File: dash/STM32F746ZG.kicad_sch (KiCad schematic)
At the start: 84 parts, among them J1 XF2M-4015-1A, J2 CLP-103-02-F-D, J4 TC2030, J5 MEM2061-01-188-00-A, J6 USB_C_Receptacle_USB2.0_16P, SW1 SW_SPST, SW2 PTS647Sx38, SW3 PTS647Sx38, U1 W9812G6KH-5, U2 STM32F746ZGTx, U7 XPT2046TS, Y2 25MHz

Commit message: nearly finished?
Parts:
- SW2, SW3: value PTS647Sx38 -> KMR221G LFS; footprint Button_Switch_SMD:SW_SPST_PTS647_Sx38 -> Button_Switch_SMD:SW_Push_1P1T_NO_CK_KMR2
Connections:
- net ~{USB_FAULT}: now also U2.80 (PD11); no longer U2.74 (PB13)
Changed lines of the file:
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@@
 	)
 	(no_connect
-		(at 370.84 219.71)
+		(at 304.8 92.71)
 	)
 	(no_connect
-		(at 304.8 92.71)
+		(at 370.84 138.43)
 	)
 	(no_connect
@@
 	(wire
 		(pts
+			(xy 370.84 219.71) (xy 377.19 219.71)
+		)
+		(stroke
+			(width 0)
+			(type default)
+		)
+	)
+	(wire
+		(pts
 			(xy 62.23 100.33) (xy 69.85 100.33)
 		)
@@
 	(wire
 		(pts
-			(xy 370.84 138.43) (xy 377.19 138.43)
-		)
-		(stroke
-			(width 0)
-			(type default)
-		)
-	)
-	(wire
-		(pts
 			(xy 377.19 168.91) (xy 370.84 168.91)
 		)
@@
 	(global_label "~{USB_FAULT}"
 		(shape input)
-		(at 377.19 138.43 0)
+		(at 377.19 219.71 0)
 		(fields_autoplaced yes)
 		(effects
@@
 		)
 		(property "Intersheetrefs" "${INTERSHEET_REFS}"
-			(at 389.802 138.43 0)
+			(at 389.802 219.71 0)
 			(effects
 				(font
@@
 			)
 		)
-		(property "Value" "PTS647Sx38"
+		(property "Value" "KMR221G LFS"
 			(at 270.383 278.638 90)
 			(effects
@@
 			)
 		)
-		(property "Footprint" "Button_Switch_SMD:SW_SPST_PTS647_Sx38"
+		(property "Footprint" "Button_Switch_SMD:SW_Push_1P1T_NO_CK_KMR2"
 			(at 276.86 267.97 0)
 			(effects
@@
 			)
 		)
-		(property "Value" "PTS647Sx38"
+		(property "Value" "KMR221G LFS"
 			(at 213.233 50.038 90)
 			(effects
@@
 			)
 		)
-		(property "Footprint" "Button_Switch_SMD:SW_SPST_PTS647_Sx38"
+		(property "Footprint" "Button_Switch_SMD:SW_Push_1P1T_NO_CK_KMR2"
 			(at 219.71 39.37 0)
 			(effects

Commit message: final stretch
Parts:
- SW1: footprint Button_Switch_SMD:SW_DIP_SPSTx01_Slide_Omron_A6S-110x_W8.9mm_P2.54mm -> Temp:A6T-1101
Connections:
- net user_button: now also U2.21 (PF9)
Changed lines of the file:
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@@
 	)
 	(no_connect
+		(at 370.84 82.55)
+	)
+	(no_connect
 		(at 370.84 201.93)
 	)
@@
 	)
 	(no_connect
-		(at 304.8 153.67)
-	)
-	(no_connect
 		(at 54.61 41.91)
 	)
@@
 	(wire
 		(pts
-			(xy 375.92 82.55) (xy 370.84 82.55)
+			(xy 184.15 254) (xy 184.15 256.54)
 		)
 		(stroke
@@
 	(wire
 		(pts
-			(xy 184.15 254) (xy 184.15 256.54)
+			(xy 186.69 166.37) (xy 186.69 184.15)
 		)
 		(stroke
@@
 	(wire
 		(pts
-			(xy 186.69 166.37) (xy 186.69 184.15)
+			(xy 377.19 133.35) (xy 370.84 133.35)
 		)
 		(stroke
@@
 	(wire
 		(pts
-			(xy 377.19 133.35) (xy 370.84 133.35)
+			(xy 204.47 118.11) (xy 228.6 118.11)
 		)
 		(stroke
@@
 	(wire
 		(pts
-			(xy 204.47 118.11) (xy 228.6 118.11)
+			(xy 102.87 224.79) (xy 105.41 224.79)
 		)
 		(stroke
@@
 	(wire
 		(pts
-			(xy 102.87 224.79) (xy 105.41 224.79)
+			(xy 332.74 44.45) (xy 335.28 44.45)
 		)
 		(stroke
@@
 	(wire
 		(pts
-			(xy 332.74 44.45) (xy 335.28 44.45)
+			(xy 378.46 97.79) (xy 370.84 97.79)
 		)
 		(stroke
@@
 	(wire
 		(pts
-			(xy 378.46 97.79) (xy 370.84 97.79)
+			(xy 298.45 153.67) (xy 304.8 153.67)
 		)
 		(stroke
@@
 		)
 	)
-	(label "user_button"
-		(at 284.48 262.89 0)
-		(effects
-			(font
-				(size 1.27 1.27)
-				(thickness 0.1588)
-			)
-			(justify left bottom)
-		)
-	)
 	(label "SWDIO"
 		(at 165.1 66.04 180)
@@
 		)
 	)
+	(label "user_button"
+		(at 284.48 262.89 0)
+		(effects
+			(font
+				(size 1.27 1.27)
+				(thickness 0.1588)
+			)
+			(justify left bottom)
+		)
+	)
 	(label "nRESET"
 		(at 157.48 38.1 180)
@@
 		)
 	)
+	(label "user_button"
+		(at 298.45 153.67 180)
+		(effects
+			(font
+				(size 1.27 1.27)
+				(thickness 0.1588)
+			)
+			(justify right bottom)
+		)
+	)
 	(label "OSC_OUT"
 		(at 298.45 82.55 180)
@@
 			)
 		)
-		(property "Footprint" "Button_Switch_SMD:SW_DIP_SPSTx01_Slide_Omron_A6S-110x_W8.9mm_P2.54mm"
+		(property "Footprint" "Temp:A6T-1101"
 			(at 208.28 67.31 0)
 			(effects

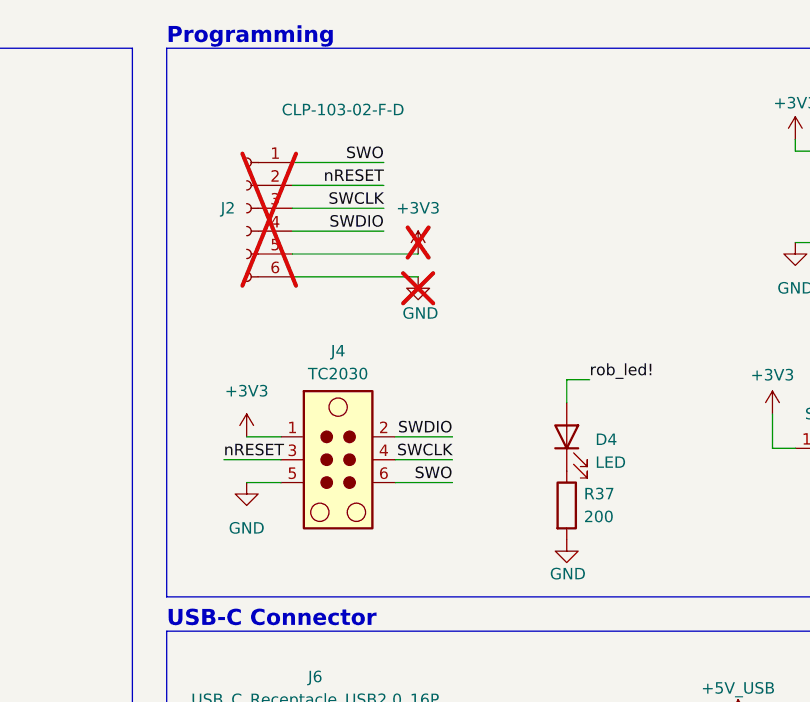
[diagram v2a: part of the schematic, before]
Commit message: changed connector for programming
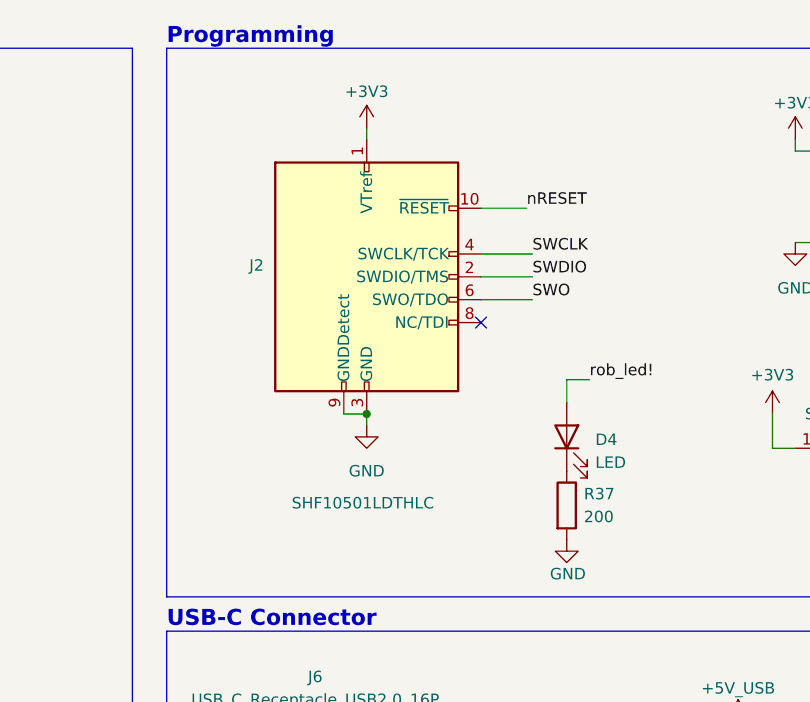
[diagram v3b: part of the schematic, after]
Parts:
- removed J2: CLP-103-02-F-D, symbol Connector:Conn_01x06_Socket
- removed J4: TC2030, Connector:Tag-Connect_TC2030-IDC-FP_2x03_P1.27mm_Vertical, symbol Connector:TC2030
- added J2: SHF10501LDTHLC, SUFST:SHF10501LDTHLC, symbol Connector:Conn_ARM_JTAG_SWD_10
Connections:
- net +3V3: now also J2.1 (VTref)
- net GND: now also J2.3 (GND), J2.5 (GND), J2.9 (GNDDetect)
- net SWCLK: now also J2.4 (SWCLK/TCK)
- net SWDIO: now also J2.2 (SWDIO/TMS)
- net SWO: now also J2.6 (SWO/TDO)
- net nRESET: now also J2.10 (~{RESET})
- no-connect marks 37 -> 38

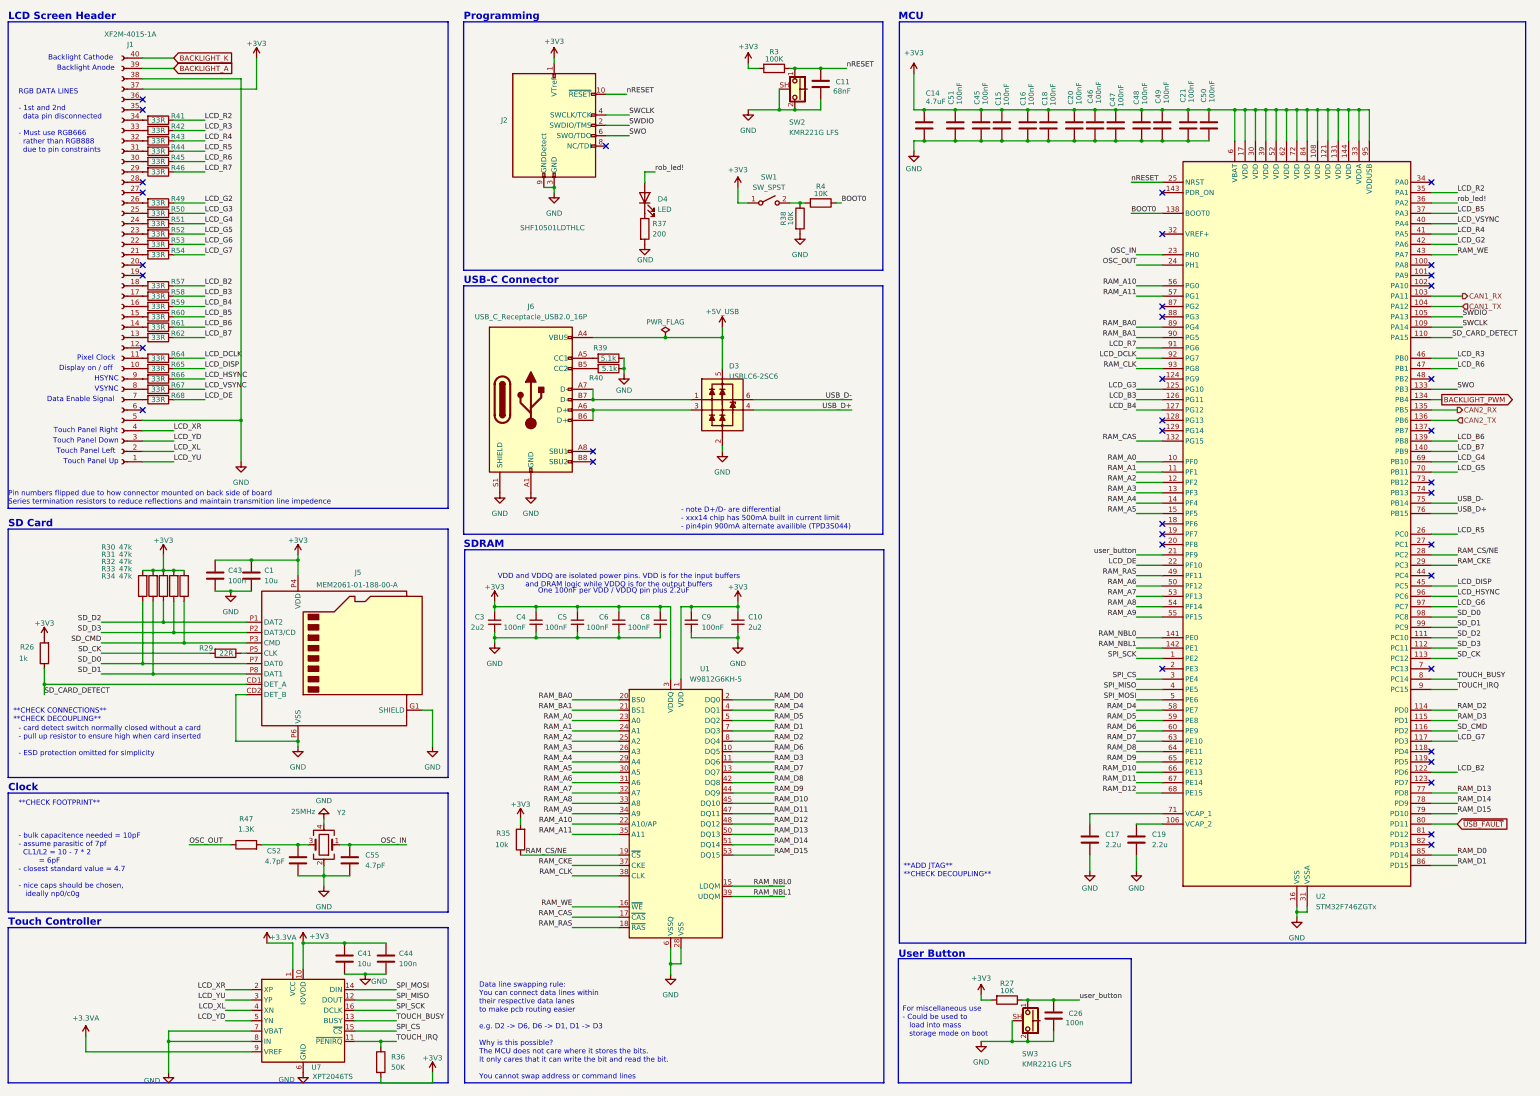
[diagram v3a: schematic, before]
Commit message: Reassigned footprints among other changes
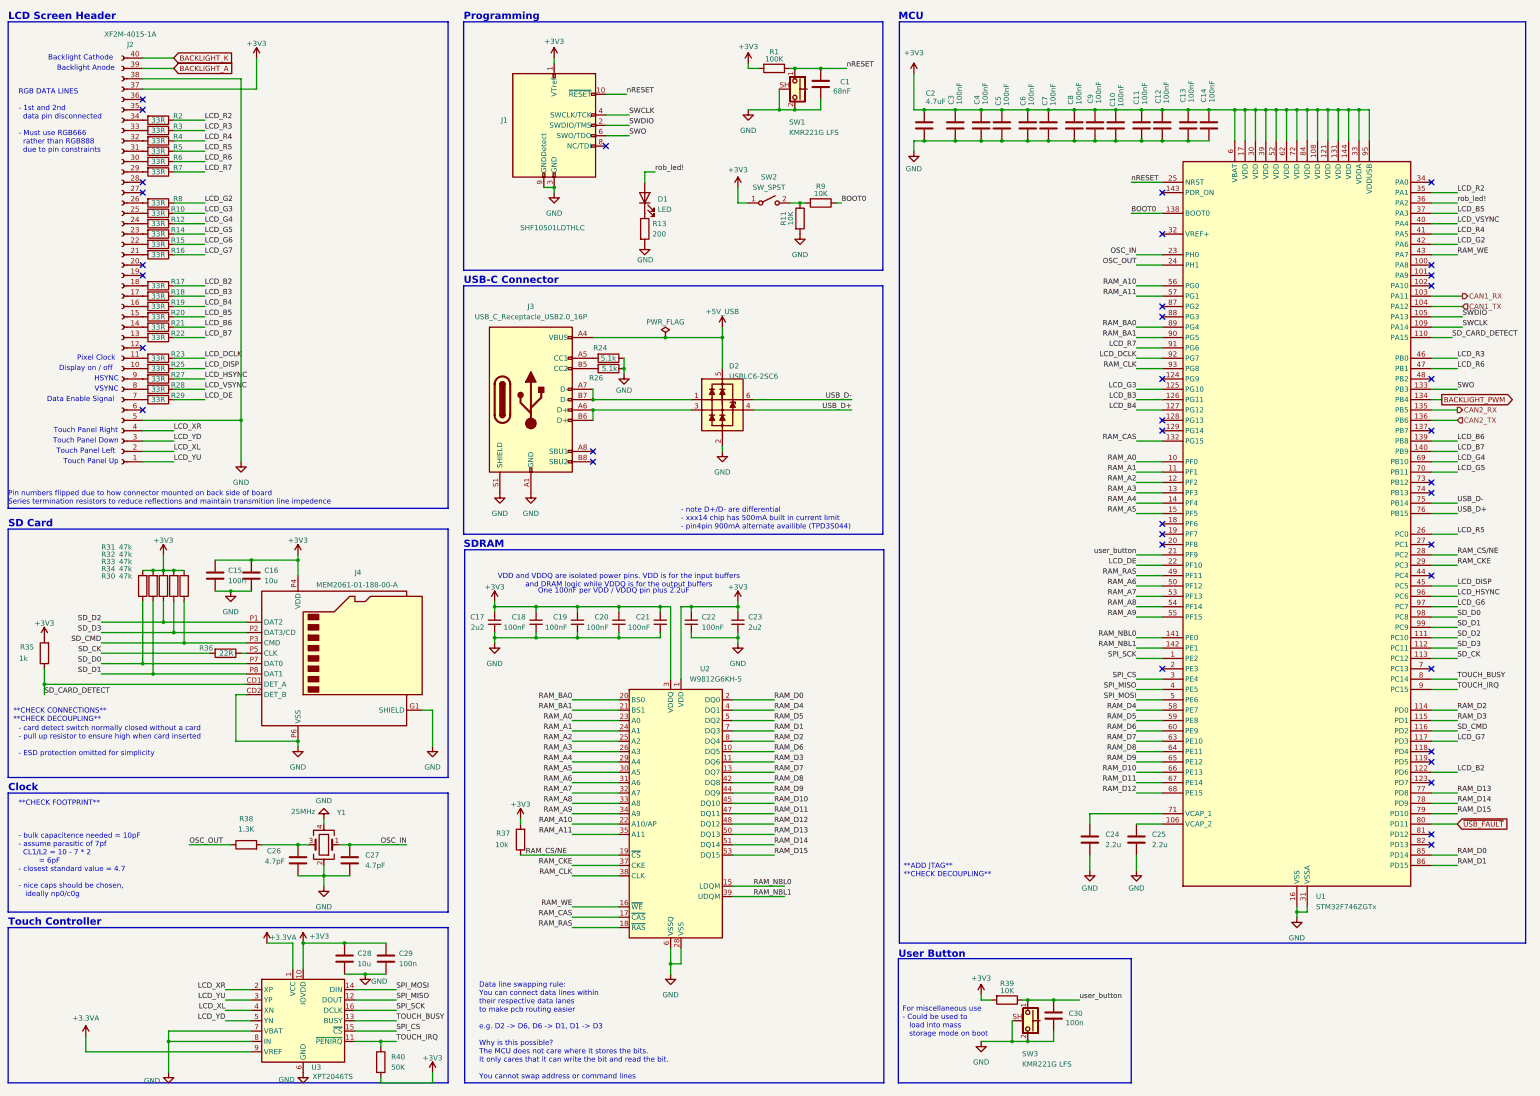
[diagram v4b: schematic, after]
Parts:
- renumbered C11 to C1, C47 to C10, C48 to C11, C49 to C12, C21 to C13, C50 to C14, C43 to C15, C1 to C16, C3 to C17, C4 to C18, C5 to C19, C14 to C2, C6 to C20, C8 to C21, C9 to C22, C10 to C23, C17 to C24, C19 to C25, C52 to C26, C55 to C27, C41 to C28, C44 to C29, C51 to C3, C26 to C30, C45 to C4, C15 to C5, C16 to C6, C18 to C7, C20 to C8, C46 to C9, D4 to D1, D3 to D2, J2 to J1, J1 to J2, J6 to J3, J5 to J4, R3 to R1, R50 to R10, R38 to R11, R51 to R12, R37 to R13, R52 to R14, R53 to R15, R54 to R16, R57 to R17, R58 to R18, R59 to R19, R41 to R2, R60 to R20, R61 to R21, R62 to R22, R64 to R23, R39 to R24, R65 to R25, R40 to R26, R66 to R27, R67 to R28, R68 to R29, R42 to R3, R34 to R30, R30 to R31, R31 to R32, R32 to R33, R33 to R34, R26 to R35, R29 to R36, R35 to R37, R47 to R38, R27 to R39, R43 to R4, R36 to R40, R44 to R5, R45 to R6, R46 to R7, R49 to R8, R4 to R9, SW2 to SW1, SW1 to SW2, U2 to U1, U1 to U2, U7 to U3, Y2 to Y1

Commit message: finishing layout
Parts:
- J1: footprint SUFST:SHF10501LDTHLC -> SUFST:SHF10501LDSMLC
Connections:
- net GND: no longer SW1.SH (B), SW3.SH (B)
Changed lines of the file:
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@@
 	(rectangle
 		(start 21.59 245.11)
-		(end 129.54 283.21)
+		(end 129.54 284.48)
 		(stroke
 			(width 0)
@@
 	)
 	(junction
-		(at 267.97 273.05)
-		(diameter 0)
-		(color 0 0 0 0)
-	)
-	(junction
 		(at 325.12 44.45)
 		(diameter 0)
@@
 	)
 	(junction
-		(at 210.82 44.45)
-		(diameter 0)
-		(color 0 0 0 0)
-	)
-	(junction
 		(at 64.77 175.26)
 		(diameter 0)
@@
 	(wire
 		(pts
-			(xy 210.82 44.45) (xy 214.63 44.45)
+			(xy 203.2 44.45) (xy 214.63 44.45)
 		)
 		(stroke
@@
 	(wire
 		(pts
-			(xy 267.97 273.05) (xy 271.78 273.05)
-		)
-		(stroke
-			(width 0)
-			(type default)
-		)
-	)
-	(wire
-		(pts
 			(xy 160.02 199.39) (xy 171.45 199.39)
 		)
@@
 	(wire
 		(pts
-			(xy 260.35 273.05) (xy 267.97 273.05)
+			(xy 260.35 273.05) (xy 271.78 273.05)
 		)
 		(stroke
@@
 	(wire
 		(pts
-			(xy 203.2 44.45) (xy 210.82 44.45)
-		)
-		(stroke
-			(width 0)
-			(type default)
-		)
-	)
-	(wire
-		(pts
 			(xy 92.71 154.94) (xy 92.71 158.75)
 		)
@@
 	(wire
 		(pts
-			(xy 210.82 39.37) (xy 210.82 44.45)
-		)
-		(stroke
-			(width 0)
-			(type default)
-		)
-	)
-	(wire
-		(pts
 			(xy 93.98 248.92) (xy 104.14 248.92)
 		)
@@
 	(wire
 		(pts
-			(xy 267.97 267.97) (xy 267.97 273.05)
-		)
-		(stroke
-			(width 0)
-			(type default)
-		)
-	)
-	(wire
-		(pts
 			(xy 377.19 179.07) (xy 370.84 179.07)
 		)
@@
 		(pin "2"
 		)
-		(pin "SH"
-		)
 		(instances
 			(project "Dashboard"
@@
 	)
 	(symbol
+		(lib_name "CK_KMS2xxG_1")
 		(lib_id "Switch:CK_KMS2xxG")
 		(at 214.63 39.37 270)
@@
 		(pin "2"
 		)
-		(pin "SH"
-		)
 		(instances
 			(project "Dashboard"
@@
 			)
 		)
-		(property "Footprint" "SUFST:SHF10501LDTHLC"
+		(property "Footprint" "SUFST:SHF10501LDSMLC"
 			(at 155.575 48.26 0)
 			(effects

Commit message: Reviewing with anna
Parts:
- R13: value 200 -> 500R
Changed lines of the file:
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@@
 			)
 		)
-		(property "Value" "200"
+		(property "Value" "500R"
 			(at 179.705 74.9299 0)
 			(effects

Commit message: Reviewing and changing
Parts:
- added JP3: SolderJumper_3_Bridged12, Jumper:SolderJumper-3_P1.3mm_Bridged2Bar12_RoundedPad1.0x1.5mm, symbol Jumper:SolderJumper_3_Bridged12
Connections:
- net +3V3: now also JP3.3 (B)
- net GND: now also JP3.1 (A)
- net BOOT1: now reaches U1.48 (PB2)
- net BOOT1: now also JP3.2 (C)
- no-connect marks 38 -> 37
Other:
- moved on the sheet: D1, J1, R13

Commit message: Adding silkscreen, cleaning up DRC
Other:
- moved on the sheet: J1
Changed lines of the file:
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@@
 	(text "For miscellaneous use\n- Could be used to\n   load into mass\n   storage mode on boot"
 		(exclude_from_sim no)
-		(at 241.046 268.224 0)
+		(at 241.3 267.97 0)
 		(effects
 			(font
@@
 	(text "User Button"
 		(exclude_from_sim no)
-		(at 240.03 251.714 0)
+		(at 240.03 251.46 0)
 		(effects
 			(font
@@
 	)
 	(junction
-		(at 149.225 60.325)
+		(at 149.86 60.96)
 		(diameter 0)
 		(color 0 0 0 0)
@@
 	)
 	(no_connect
-		(at 161.925 50.165)
+		(at 162.56 50.8)
 	)
 	(no_connect
@@
 	(wire
 		(pts
-			(xy 167.64 45.085) (xy 161.925 45.085)
+			(xy 167.64 45.72) (xy 162.56 45.72)
 		)
 		(stroke
@@
 	(wire
 		(pts
-			(xy 167.64 42.545) (xy 161.925 42.545)
+			(xy 167.64 43.18) (xy 162.56 43.18)
 		)
 		(stroke
@@
 	(wire
 		(pts
-			(xy 149.225 60.325) (xy 149.225 61.595)
+			(xy 149.86 60.96) (xy 149.86 62.23)
 		)
 		(stroke
@@
 	(wire
 		(pts
-			(xy 146.685 60.325) (xy 149.225 60.325)
+			(xy 147.32 60.96) (xy 149.86 60.96)
 		)
 		(stroke
@@
 	(wire
 		(pts
-			(xy 167.005 37.465) (xy 161.925 37.465)
+			(xy 167.64 38.1) (xy 162.56 38.1)
 		)
 		(stroke
@@
 	(wire
 		(pts
-			(xy 149.225 29.845) (xy 149.225 28.575)
+			(xy 149.86 30.48) (xy 149.86 29.21)
 		)
 		(stroke
@@
 	(wire
 		(pts
-			(xy 167.64 47.625) (xy 161.925 47.625)
+			(xy 167.64 48.26) (xy 162.56 48.26)
 		)
 		(stroke
@@
 	)
 	(label "SWCLK"
-		(at 167.64 42.545 0)
+		(at 167.64 43.18 0)
 		(effects
 			(font
@@
 	)
 	(label "SWDIO"
-		(at 167.64 45.085 0)
+		(at 167.64 45.72 0)
 		(effects
 			(font
@@
 	)
 	(label "nRESET"
-		(at 167.005 37.465 0)
+		(at 167.64 38.1 0)
 		(effects
 			(font
@@
 	)
 	(label "SWO"
-		(at 167.64 47.625 0)
+		(at 167.64 48.26 0)
 		(effects
 			(font
@@
 		(length 2.54)
 		(shape round)
-		(at 80.645 50.165 270)
+		(at 80.645 50.8 270)
 		(fields_autoplaced yes)
 		(effects
@@
 		)
 		(property "Netclass" "LCD"
-			(at 83.185 49.5554 90)
+			(at 83.185 50.1904 90)
 			(effects
 				(font
@@
 		)
 		(property "Component Class" ""
-			(at -168.91 -90.17 0)
+			(at -168.91 -89.535 0)
 			(effects
 				(font
@@
 	(symbol
 		(lib_id "power:+3V3")
-		(at 149.225 28.575 0)
+		(at 149.86 29.21 0)
 		(unit 1)
 		(exclude_from_sim no)
@@
 		(dnp no)
 		(property "Reference" "#PWR03"
-			(at 149.225 32.385 0)
+			(at 149.86 33.02 0)
 			(effects
 				(font
@@
 		)
 		(property "Value" "+3V3"
-			(at 149.225 24.511 0)
+			(at 149.86 25.146 0)
 			(effects
 				(font
@@
 		)
 		(property "Footprint" ""
-			(at 149.225 28.575 0)
+			(at 149.86 29.21 0)
 			(effects
 				(font
@@
 		)
 		(property "Datasheet" ""
-			(at 149.225 28.575 0)
+			(at 149.86 29.21 0)
 			(effects
 				(font
@@
 		)
 		(property "Description" "Power symbol creates a global label with name \"+3V3\""
-			(at 149.225 28.575 0)
+			(at 149.86 29.21 0)
 			(effects
 				(font
@@
 	(symbol
 		(lib_id "Connector:Conn_ARM_JTAG_SWD_10")
-		(at 149.225 45.085 0)
+		(at 149.86 45.72 0)
 		(unit 1)
 		(exclude_from_sim no)
@@
 		(dnp no)
 		(property "Reference" "J1"
-			(at 137.795 43.8149 0)
+			(at 138.43 44.4499 0)
 			(effects
 				(font
@@
 		)
 		(property "Value" "SHF10501LDTHLC"
-			(at 156.718 70.231 0)
+			(at 157.353 70.866 0)
 			(effects
 				(font
@@
 		)
 		(property "Footprint" "SUFST:SHF10501LDSMLC"
-			(at 149.225 45.085 0)
+			(at 149.86 45.72 0)
 			(effects
 				(font
@@
 		)
 		(property "Datasheet" "http://infocenter.arm.com/help/topic/com.arm.doc.ddi0314h/DDI0314H_coresight_components_trm.pdf"
-			(at 140.335 76.835 90)
+			(at 140.97 77.47 90)
 			(effects
 				(font
@@
 		)
 		(property "Description" "Cortex Debug Connector, standard ARM Cortex-M SWD and JTAG interface"
-			(at 149.225 45.085 0)
+			(at 149.86 45.72 0)
 			(effects
 				(font
@@
 	(symbol
 		(lib_id "power:GND")
-		(at 149.225 61.595 0)
+		(at 149.86 62.23 0)
 		(mirror y)
 		(unit 1)
@@
 		(fields_autoplaced yes)
 		(property "Reference" "#PWR09"
-			(at 149.225 67.945 0)
+			(at 149.86 68.58 0)
 			(effects
 				(font
@@
 		)
 		(property "Value" "GND"
-			(at 149.225 66.675 0)
+			(at 149.86 67.31 0)
 			(effects
 				(font
@@
 		)
 		(property "Footprint" ""
-			(at 149.225 61.595 0)
+			(at 149.86 62.23 0)
 			(effects
 				(font
@@
 		)
 		(property "Datasheet" ""
-			(at 149.225 61.595 0)
+			(at 149.86 62.23 0)
 			(effects
 				(font
@@
 		)
 		(property "Description" "Power symbol creates a global label with name \"GND\" , ground"
-			(at 149.225 61.595 0)
+			(at 149.86 62.23 0)
 			(effects
 				(font
